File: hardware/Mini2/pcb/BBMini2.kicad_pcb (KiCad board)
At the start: 2 copper layers, 123 x 91 mm, 73 parts, among them J1 Schurter_CMF1, J2 USB_A, J3 Display, Q1 MBT2222ADW1T1, SW1 SW_Push, SW2 SW_Push, SW3 SW_Push, U1 ESP8266EX, U2 AT25DF041x-UxN-x, U3 AP2112K-3.3, U4 CP2104, U5 MCP3208, Y1 ABM8-26.000MHZ-10-1-U-T

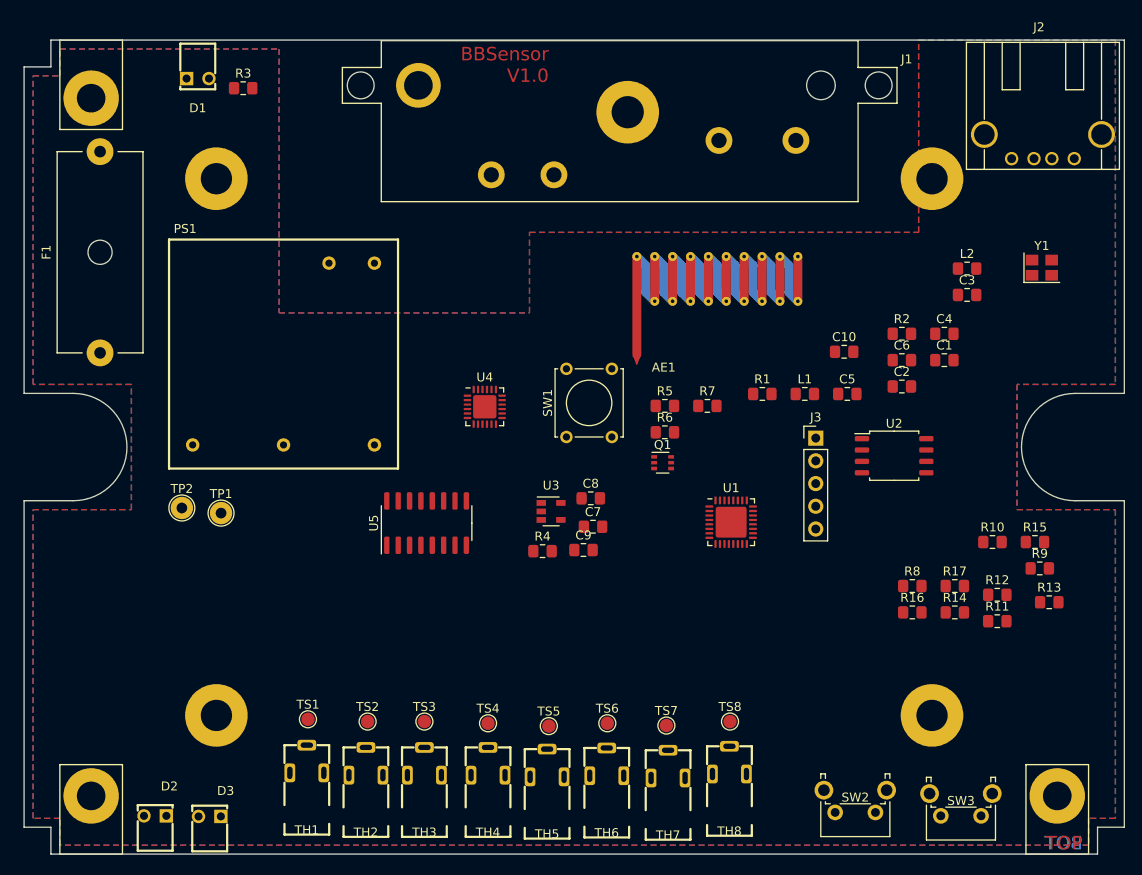
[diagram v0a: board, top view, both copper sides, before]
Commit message: feat: BBMini2 - experimental ESP8266 PCB (SMD)
* shrink PCB, switch components

Issue #23
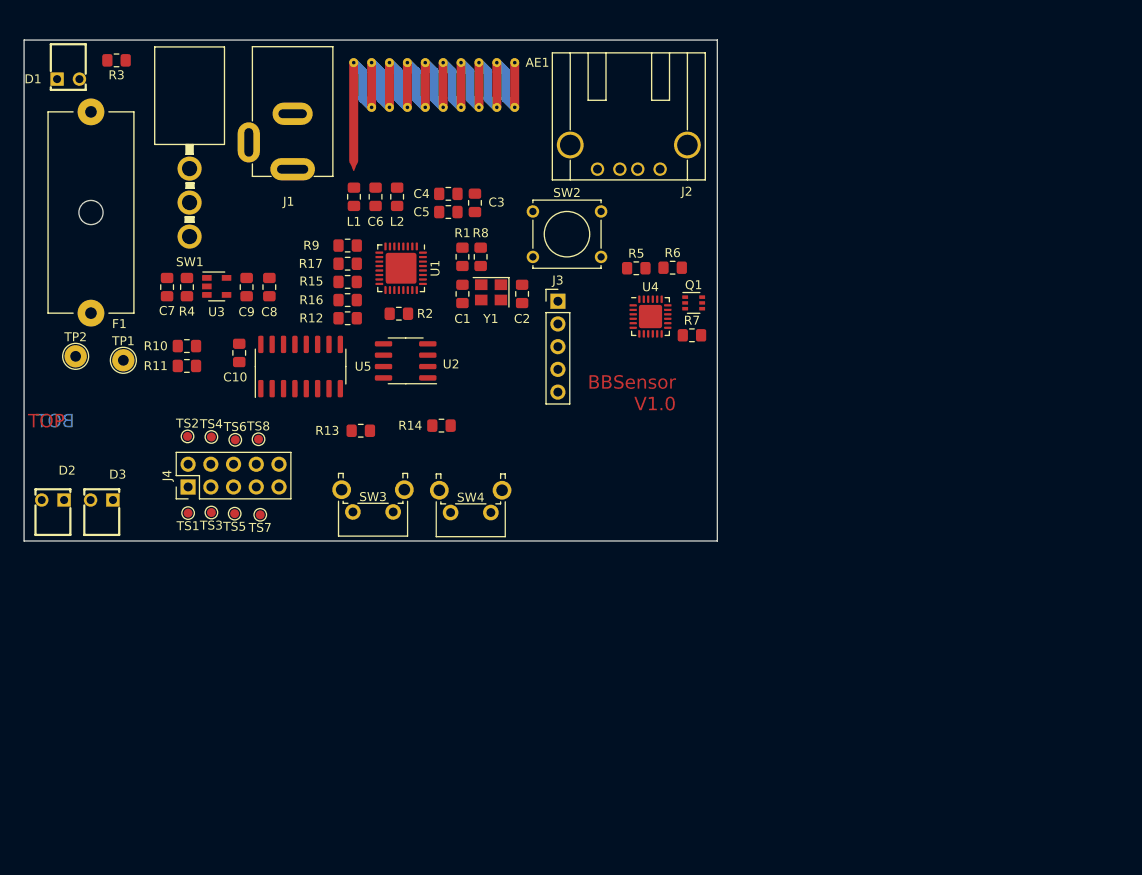
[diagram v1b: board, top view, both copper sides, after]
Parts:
- removed PS1: TMPS_05, Traco:Traco_TMPS_05
- removed TH1, TH2, TH3, TH4, TH5, TH6, TH7, TH8: AudioJack3, Lumberg:LUMBERG_1501_05
- removed ~ (x3): Mounting_Bracket_L10_W7_M3, Collection:Mounting_Bracket_L10_W7_M3
- removed ~ (x4): ~, MountingHole:MountingHole_3.5mm_Pad
- added J4: Conn_02x05_Odd_Even, Connector_PinHeader_2.54mm:PinHeader_2x05_P2.54mm_Vertical, F.Cu at (33.3, 65.0)
- added SW1: SW_SPDT, Collection:MIYAMA_MS-500-B-VT, F.Cu at (37.4, 26.7)
- J1: value Schurter_CMF1 -> Barrel_Jack_Switch; footprint Schurter:CMF1_Offset -> Lumberg:LUMBERG_NEB_21R
- TS1, TS2, TS3, TS4, TS5, TS6, TS7, TS8: footprint TestPoint:TestPoint_Pad_D1.5mm -> TestPoint:TestPoint_Pad_D1.0mm
- U2: value AT25DF041x-UxN-x -> AT25SF081-SSHF-X; footprint Package_SO:SOIC-8_5.275x5.275mm_P1.27mm -> Package_SO:SOIC-8_3.9x4.9mm_P1.27mm
- moved R11 95.0 mm to (33.2, 51.4)
- moved R10 92.7 mm to (33.2, 49.2)
- moved R9 85.4 mm to (51.2, 38.0)
- moved R15 82.2 mm to (51.2, 42.0)
- moved R13 79.3 mm to (52.6, 58.7)
- moved R12 78.9 mm to (51.2, 46.1)
- moved R17 76.8 mm to (51.2, 40.0), turned to 180 degrees
- moved R16 72.1 mm to (51.2, 44.1), turned to 180 degrees
- moved C10 67.6 mm to (39.1, 50.0), turned to 270 degrees
- moved SW4 64.4 mm to (67.2, 67.8)
- moved L2 64.2 mm to (56.7, 32.5), turned to 90 degrees
- moved SW3 63.5 mm to (56.3, 67.8)
- moved Y1 61.6 mm to (67.2, 43.2), turned to 180 degrees
- moved C6 61.6 mm to (54.3, 32.5), turned to 270 degrees
- moved TS8 61.4 mm to (41.2, 59.6)
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- renumbered SW1 to SW2, SW2 to SW3, SW3 to SW4
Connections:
- net Net-(C1-Pad2) renamed /ESP8266EX/XTAL_OUT
- net Net-(C2-Pad2) renamed /ESP8266EX/XTAL_IN
- net Net-(C6-Pad2) renamed /ESP8266EX/LNA
- net Net-(R2-Pad2) renamed /ESP8266EX/SDIO_CLK
- J1 pad 2: Net-(J1-Pad2) -> GND
- U1 pad 18: Net-(U1-Pad18) -> /ESP8266EX/SDIO_DATA_2
- U1 pad 19: Net-(U1-Pad19) -> /ESP8266EX/SDIO_DATA_3
- U1 pad 20: Net-(U1-Pad20) -> /ESP8266EX/SDIO_CMD
- U1 pad 22: Net-(U1-Pad22) -> /ESP8266EX/SDIO_DATA_0
- U1 pad 23: Net-(U1-Pad23) -> /ESP8266EX/SDIO_DATA_1
- U2 pad 1: (no net) -> /ESP8266EX/SDIO_CMD
- U2 pad 2: (no net) -> /ESP8266EX/SDIO_DATA_0
- U2 pad 3: (no net) -> /ESP8266EX/SDIO_DATA_3
- U2 pad 4: (no net) -> GND
- U2 pad 5: (no net) -> /ESP8266EX/SDIO_DATA_1
- U2 pad 6: (no net) -> Net-(R2-Pad1)
- U2 pad 7: (no net) -> /ESP8266EX/SDIO_DATA_2
- U2 pad 8: (no net) -> +3V3
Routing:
- removed copper zone on F.Cu, net +5V
- removed copper zone on B.Cu, net GND
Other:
- board size 123 x 91 mm -> 77.5 x 56 mm
- net class 3V3: clearance 0.2 -> 0.125; trace_width 0.3 -> 0.2; via_dia 0.8 -> 0.6; via_drill 0.4 -> 0.3
- net class Default: via_dia 0.8 -> 0.6; via_drill 0.4 -> 0.3

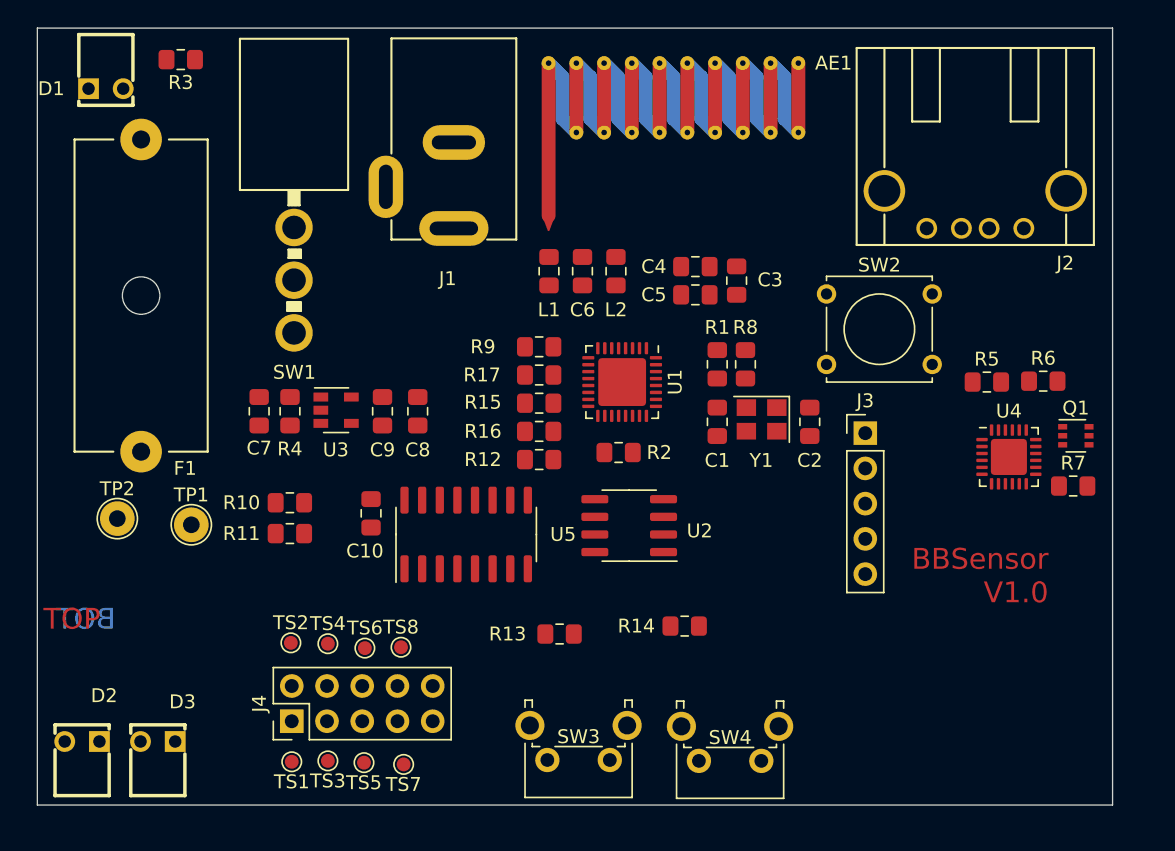
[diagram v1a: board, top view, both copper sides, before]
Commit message: feat: BBMini2 - experimental ESP8266 PCB (SMD)
make everything smaller

Issue #23
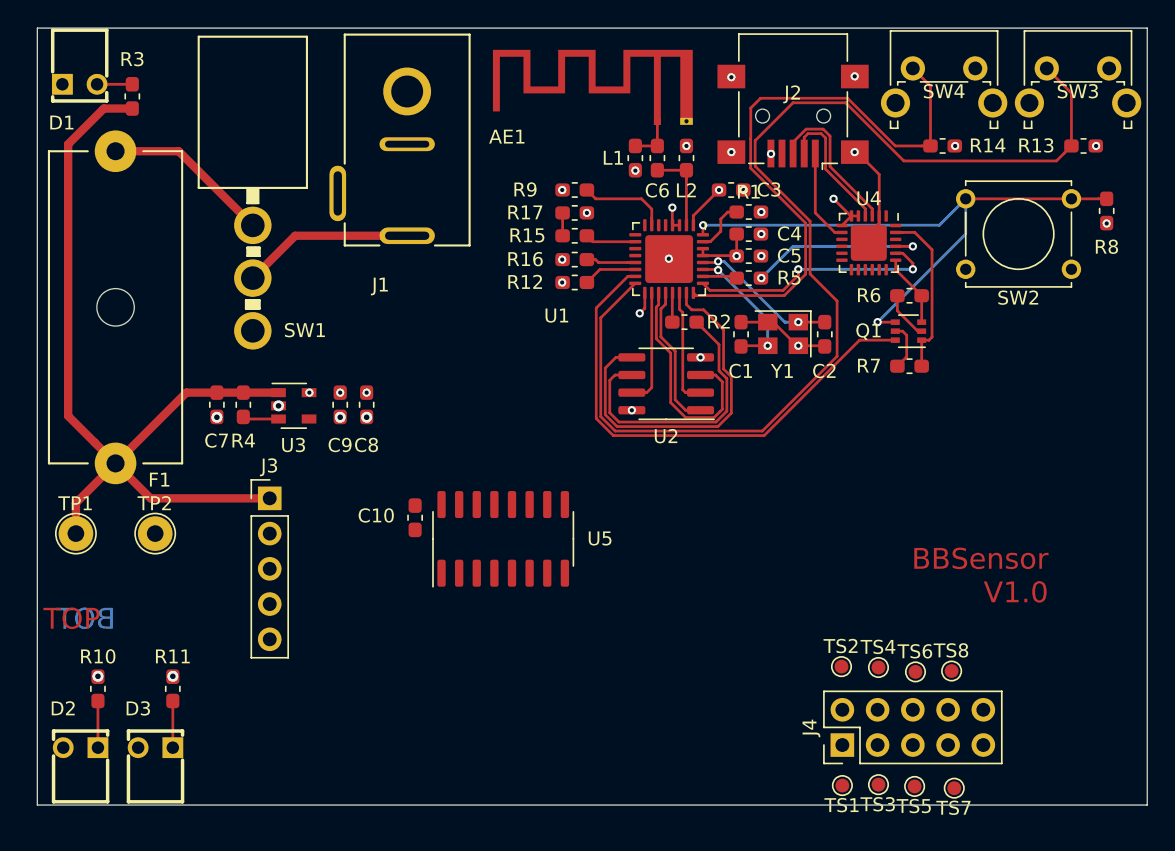
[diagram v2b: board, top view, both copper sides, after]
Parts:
- AE1: value Antenna -> Antenna_Shield; footprint RF_Antenna:Texas_SWRA416_868MHz_915MHz -> RF_Antenna:Texas_SWRA117D_2.4GHz_Left
- C1, C10, C2, C3, C4, C5, C6, C7, C8, C9: footprint Capacitor_SMD:C_0805_2012Metric_Pad1.15x1.40mm_HandSolder -> Capacitor_SMD:C_0603_1608Metric_Pad1.05x0.95mm_HandSolder
- J1: footprint Lumberg:LUMBERG_NEB_21R -> Collection:CLIFF_DC_SOCKET_2.5
- J2: value USB_A -> USB_B_Mini; footprint Lumberg:LUMBERG_2410_06 -> Connector_USB:USB_Mini-B_Lumberg_2486_01_Horizontal
- L1, L2: footprint Inductor_SMD:L_0805_2012Metric_Pad1.15x1.40mm_HandSolder -> Inductor_SMD:L_0603_1608Metric_Pad1.05x0.95mm_HandSolder
- R1, R10, R11, R12, R13, R14, R15, R16, R17, R2, R3, R4, R5, R6, R7, R8, R9: footprint Resistor_SMD:R_0805_2012Metric_Pad1.15x1.40mm_HandSolder -> Resistor_SMD:R_0603_1608Metric_Pad1.05x0.95mm_HandSolder
- moved SW3 59.0 mm to (87.8, 17.9), turned to 0 degrees
- moved R13 51.6 mm to (90.4, 23.5), turned to 180 degrees
- moved SW4 51.1 mm to (78.1, 17.9), turned to 0 degrees
- moved J3 43.2 mm to (31.8, 48.9)
- moved J4 39.7 mm to (73.0, 66.7)
- moved TS1 39.7 mm to (73.0, 69.6)
- moved TS6 39.7 mm to (78.3, 61.4)
- moved TS2 39.7 mm to (73.0, 61.0)
- moved TS3 39.7 mm to (75.6, 69.5)
- moved TS4 39.7 mm to (75.6, 61.1)
- moved TS5 39.7 mm to (78.2, 69.7)
- moved TS7 39.7 mm to (81.1, 69.8)
- moved TS8 39.7 mm to (80.9, 61.3)
- moved R14 39.3 mm to (80.2, 23.5), turned to 180 degrees
- moved R8 28.3 mm to (92.1, 28.2)
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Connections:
- J2 pad 4: GND -> Net-(J2-Pad4)
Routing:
- net /ESP8266EX/GPIO4: track 0.00 -> 80.8 mm
- net +5V: track 0.00 -> 62.4 mm
- net /ESP8266EX/~RST: track 0.00 -> 43.4 mm, vias 0 -> 2
- net /ESP8266EX/GPIO5: track 0.00 -> 43.2 mm
- net /ESP8266EX/GPIO0: track 0.00 -> 36.6 mm
- net /ESP8266EX/SDIO_DATA_1: track 0.00 -> 25.9 mm
- net Net-(R2-Pad1): track 0.00 -> 20.5 mm
- net /ESP8266EX/GPIO1_TXD: track 0.00 -> 18.2 mm, vias 0 -> 2
- net /ESP8266EX/SDIO_DATA_3: track 0.00 -> 16.6 mm
- net +3V3: track 0.00 -> 14.5 mm, vias 0 -> 14
- net GND: track 0.00 -> 14.4 mm, vias 0 -> 22
- net /Serial/USB_RX: track 0.00 -> 13.1 mm, vias 0 -> 2
- net Net-(J1-Pad1): track 0.00 -> 12.4 mm
- net /Serial/DTR: track 0.00 -> 12.2 mm
- net Net-(F1-Pad2): track 0.00 -> 12.1 mm
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- added copper zone on In1.Cu, net +3V3
- added copper zone on In2.Cu, net GND
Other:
- board size 77.5 x 56 mm -> 80 x 56 mm
- copper layers 2 -> 4
- net class AC removed
